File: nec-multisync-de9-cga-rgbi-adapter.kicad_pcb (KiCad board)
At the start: 2 copper layers, 52.1 x 34.9 mm, 8 parts, among them J1 DE9_Plug, J2 DE15_Receptacle_HighDensity, J3 DIN-8

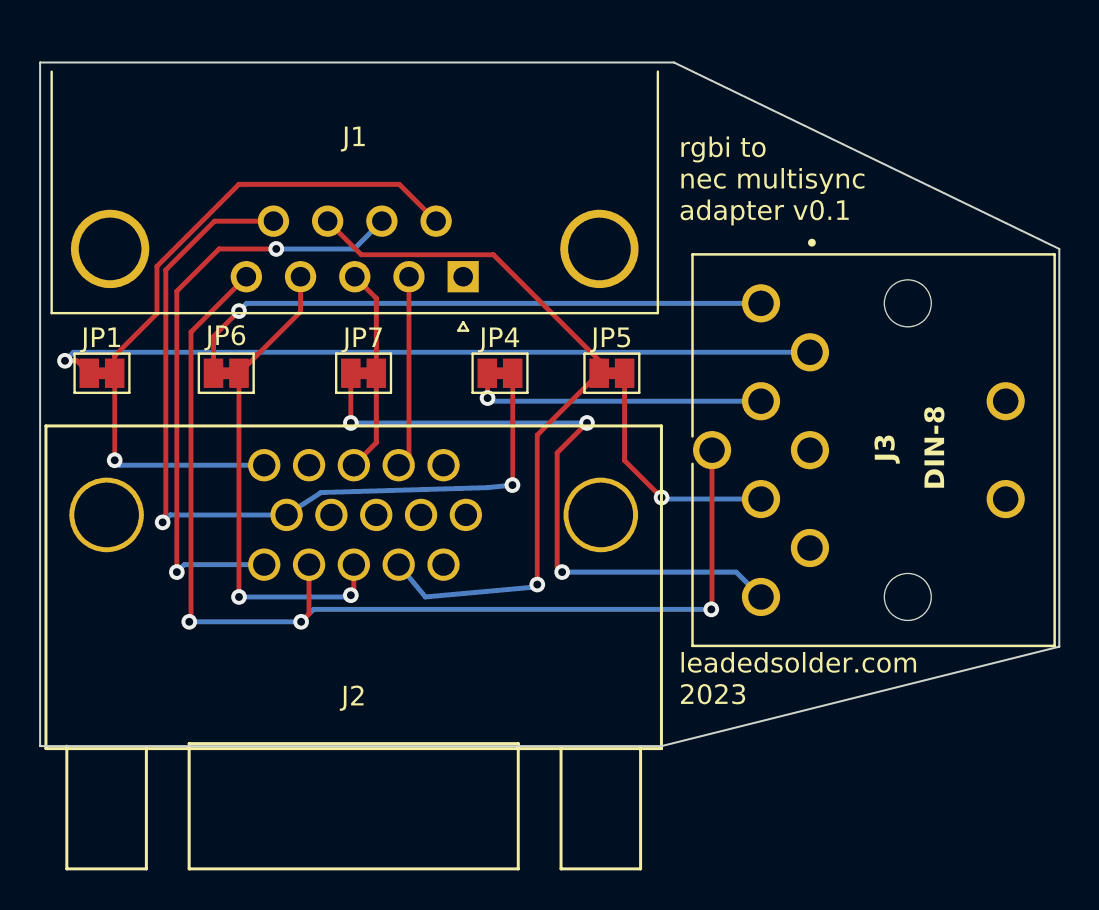
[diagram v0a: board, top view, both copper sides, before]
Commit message: Remove annoying tab that fouls on Tandy
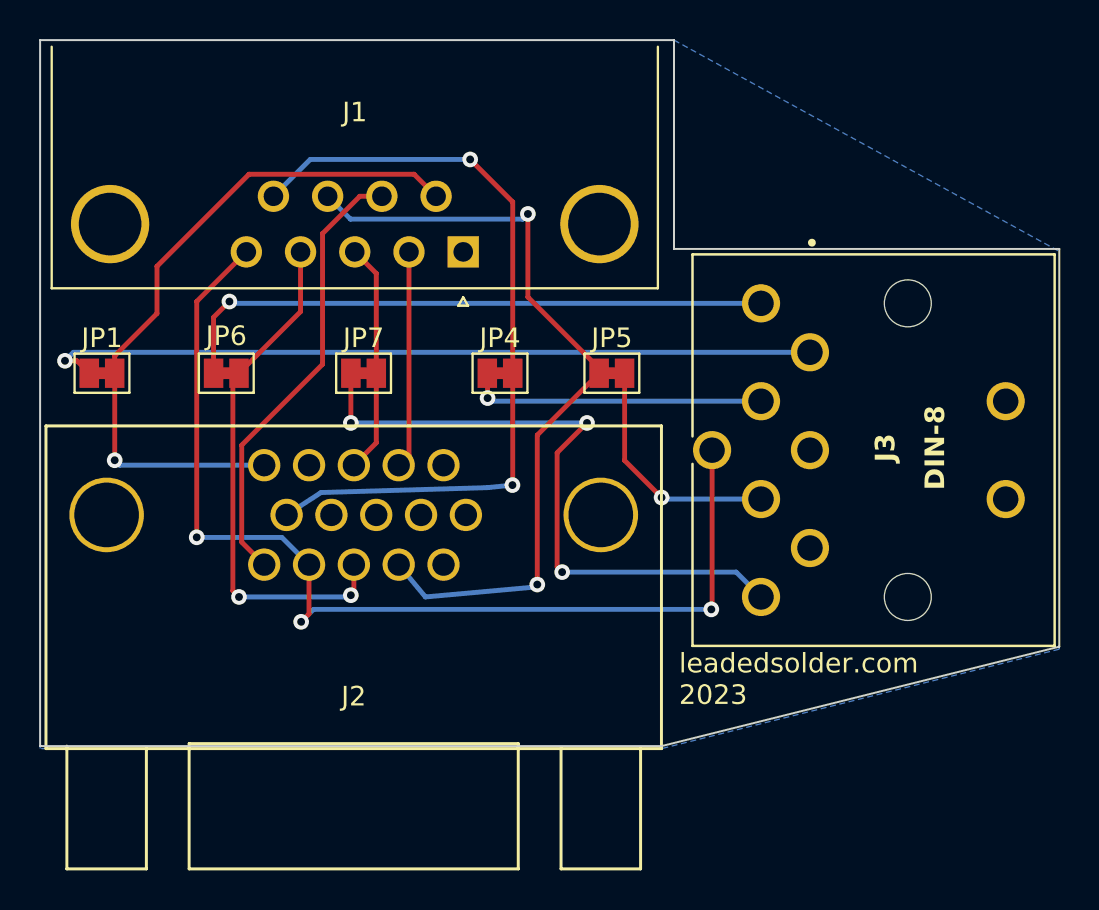
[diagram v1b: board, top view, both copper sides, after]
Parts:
- moved J1 1.27 mm to (136.6, 84.0)
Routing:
- net /EGA_Blue1: track 30.9 -> 22.9 mm, vias 2 -> 0
- net /VSync: track 43.6 -> 40.3 mm
- net /HSync: track 37.5 -> 40.5 mm, vias 1 -> 2
- net /EGA_Blue0: track 57.0 -> 54.4 mm
- net /EGA_Green0: track 25.0 -> 26.6 mm
- net /EGA_Red0: track 10.6 -> 11.8 mm
- net /EGA_Red1: track 9.85 -> 11.1 mm
- net Net-(JP6-B): track 30.5 -> 31.2 mm
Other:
- board size 52.1 x 34.9 mm -> 52.1 x 36.1 mm
- board text added: "rgbi to nec multisync adapter v0.2"
- board text removed: "rgbi to nec multisync adapter v0.1"
